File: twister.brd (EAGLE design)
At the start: 101.6 x 81.3 mm, 30 parts, among them IC1 A3967SLB, U2 ARDUINO_SHIELDNOHOLES

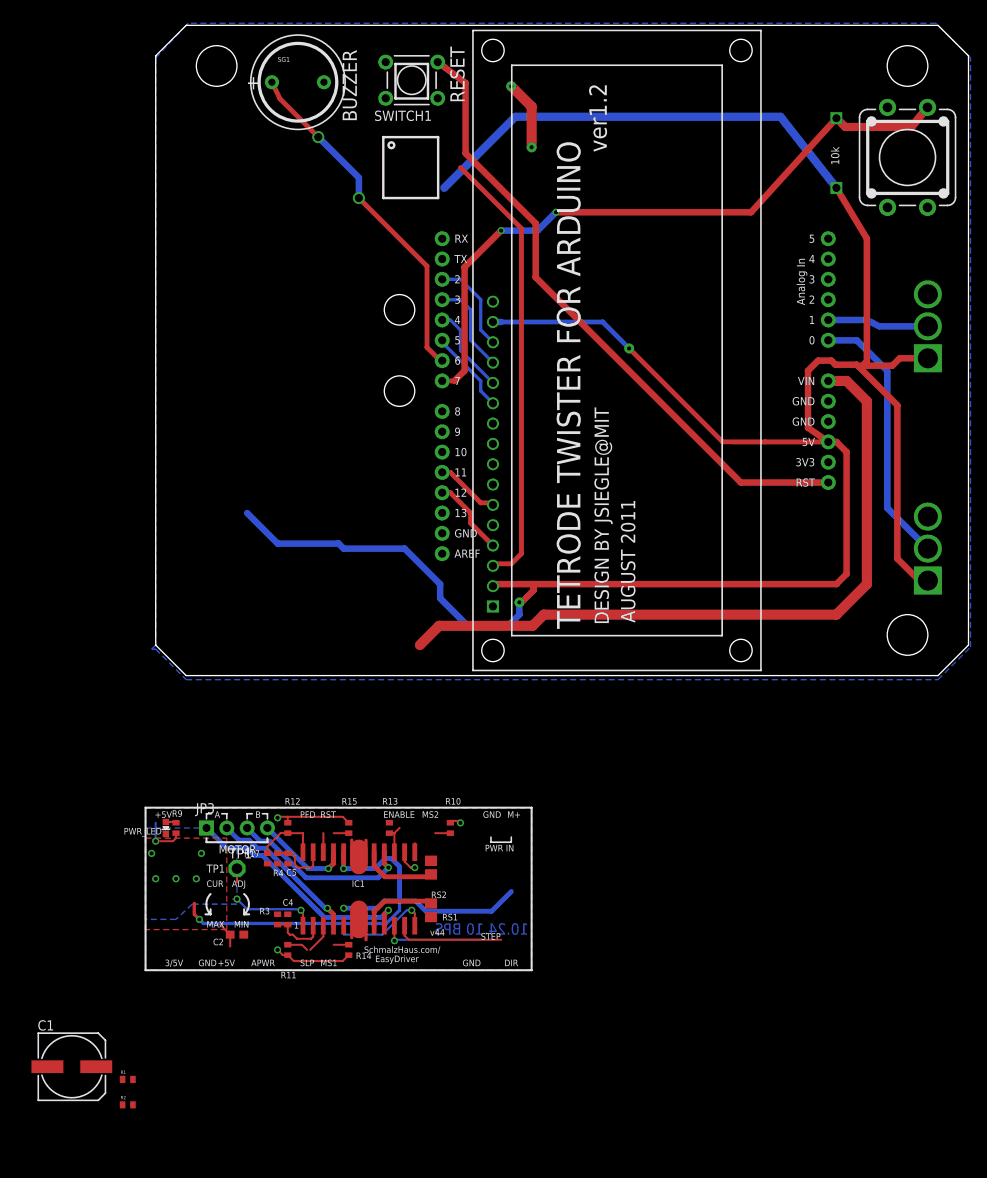
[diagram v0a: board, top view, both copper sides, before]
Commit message: Added stepper motor.
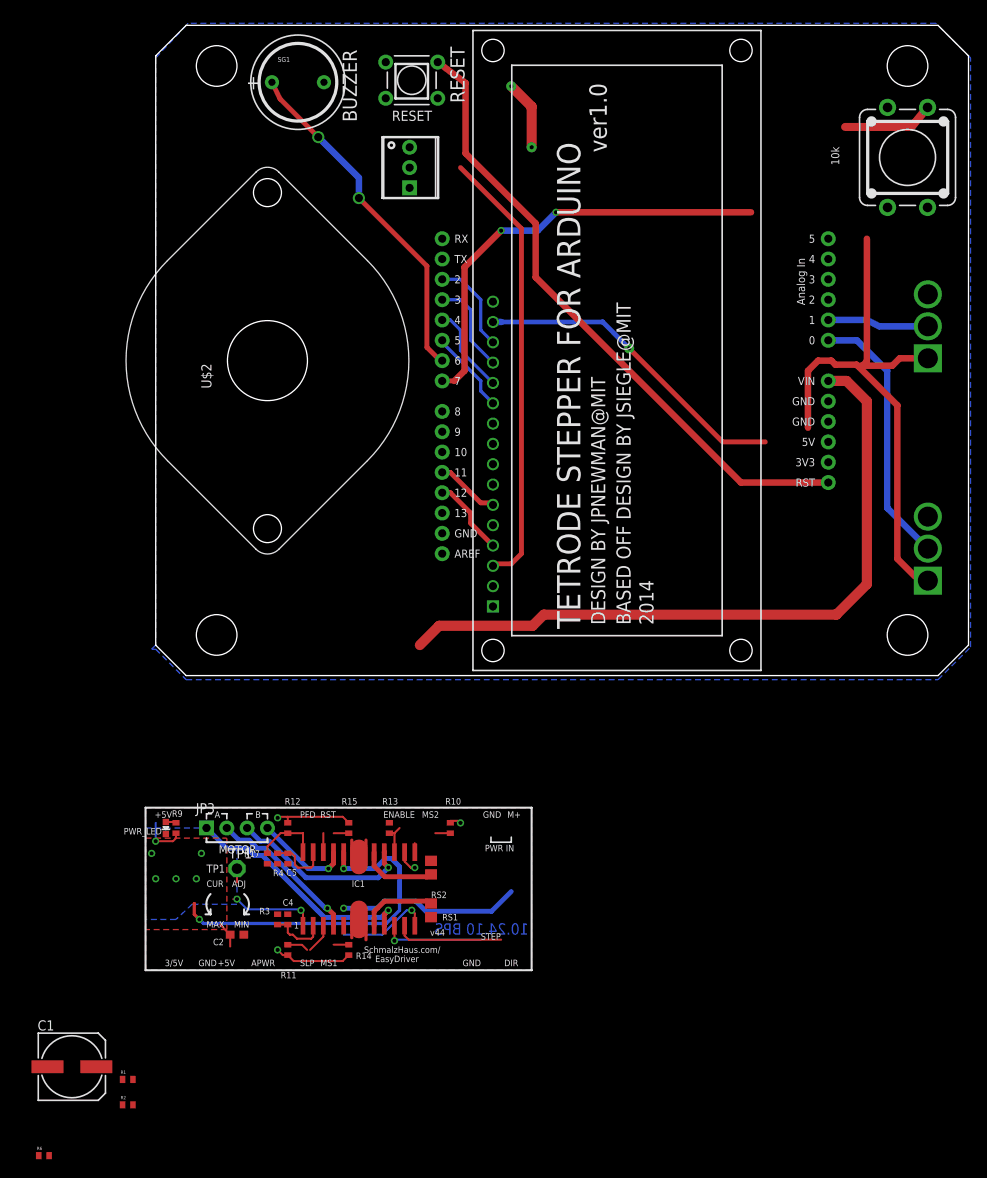
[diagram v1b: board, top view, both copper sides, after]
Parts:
- removed U$9: 10K, josh:RESISTOR
- added R56: CONTRAST, sparkfun:3362U-2
- added R6: 10K, SparkFun03_30_09:C0402
- added U$2: STEPPER_ST-PM35, twister:ST-PM35-15-11C
- RESET: value SWITCH-MOMENTARY-2PTH -> 2PTH
- S1: value SWITCH-MOMENTARY-212MM -> 212MM
- renumbered SWITCH1 to RESET
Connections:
- removed net VCC: C2.1, IC1.14, R10.2, R11.2, R12.2, R14.2, R15.2, R2.1, R9.2, U$1.15, U$10.LEFT, U$11.LEFT, U$9.P$1, U2.5V
- new net +5V: C2.1, IC1.14, R10.2, R11.2, R12.2, R14.2, R15.2, R2.1, R56.1, R6.1, R9.2, U$1.15, U$10.LEFT, U$11.LEFT
- net GND: now also R56.3
- net N$12: now also R6.2; no longer U$9.P$2
- net VO: now also R56.2
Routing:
- net VCC: track 328.3 -> 0.00 mm, vias 7 -> 0
- net +5V: track 0.00 -> 143.5 mm, vias 0 -> 6
- net N$12: track 83.8 -> 66.4 mm
- added copper zone on layer 16, net +5V
- removed copper zone on layer 16, net VCC
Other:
- board text added: "2014"
- board text added: "BASED OFF DESIGN BY JSIEGLE@MIT"
- board text added: "DESIGN BY JPNEWMAN@MIT"
- board text added: "TETRODE STEPPER FOR ARDUINO"
- board text added: "ver1.0"
- board text removed: "AUGUST 2011"
- board text removed: "DESIGN BY JSIEGLE@MIT"
- board text removed: "TETRODE TWISTER FOR ARDUINO"
- board text removed: "ver1.2"

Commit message: Everything should be set for final layout.
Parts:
- removed PWR_LED: YELLOW, SparkFun03_30_09:LED-0603
- removed R56: CONTRAST, sparkfun:3362U-2
- removed R9: 1K, SparkFun03_30_09:C0402
- removed S1: 212MM, sparkfun:TACTILE-PTH-12MM
- removed SG1: BUZZERPTH, sparkfun:BUZZER-12MM
- removed U$1: LCD-16X2, sparkfun:LCD-16X2
- removed U$2: STEPPER_ST-PM35, twister:ST-PM35-15-11C
- added BUZZER: SG1, twister_clean:BUZZER-12MM
- added CONTRAST: 10k, twister_clean:3362U-2
- added LCD_MODULE: LCD-16X2, twister_clean:LCD-16X2
- added START: 212MM, twister_clean:TACTILE-PTH-12MM
- added STEPPER: ST-PM35, twister:ST-PM35-15-11C
- C2: device rcl:C0603 -> twister_clean:0805
- C4, C5, R1, R10, R11, R12, R13, R14, R15, R17, R2, R3, R4, R6: device SparkFun03_30_09:C0402 -> twister_clean:0603
- RESET: device sparkfun:TACTILE-PTH -> twister_clean:TACTILE-PTH
- RS1, RS2: device rcl:R0805 -> twister_clean:1206
- U$10, U$11: device josh:LARGE_POT -> twister_clean:LARGE_POT
- U2: device sparkfun:DUEMILANOVE_SHIELD_NOHOLES -> twister_clean:DUEMILANOVE_SHIELD_NOHOLES
- moved C1 114.9 mm to (83.5, 17.1)
- moved RS1 51.3 mm to (29.3, 21.7), turned to 180 degrees
- moved RS2 46.9 mm to (24.0, 21.7), turned to 0 degrees
- moved R14 46.8 mm to (34.3, 11.4), turned to 0 degrees
- moved R10 46.7 mm to (19.1, 24.1), turned to 180 degrees
- moved R11 42.0 mm to (34.3, 3.81), turned to 0 degrees
- moved IC1 39.4 mm to (26.7, 12.7), turned to 90 degrees
- moved C2 37.2 mm to (32.4, -2.54), turned to 90 degrees
- moved C4 37.0 mm to (30.5, 3.81), turned to 180 degrees
- moved R13 37.0 mm to (19.1, 16.5), turned to 0 degrees
- moved R3 36.4 mm to (30.5, 2.54), turned to 0 degrees
- moved R15 30.9 mm to (19.1, 11.4), turned to 180 degrees
- moved C5 27.4 mm to (22.9, 3.81), turned to 0 degrees
- moved R4 26.5 mm to (22.9, 2.54), turned to 180 degrees
- moved R17 25.7 mm to (22.9, 1.27), turned to 180 degrees
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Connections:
- removed net N$17: PWR_LED.A, R9.1
- removed net N$24: U$1.1, U$1.5
- removed net V+: C1.+
- net +5V: now also CONTRAST.1, LCD_MODULE.15, U2.5V; no longer R56.1, R9.2, U$1.15
- net D6: now also BUZZER.-; no longer SG1.-
- net GND: now also BUZZER.+, CONTRAST.3, LCD_MODULE.1, LCD_MODULE.16, LCD_MODULE.5, START.3; no longer PWR_LED.C, R56.3, S1.3, SG1.+, U$1.16
- net N$12: now also START.1; no longer S1.1
- net N$4: now also LCD_MODULE.4; no longer U$1.4
- net N$5: now also LCD_MODULE.6; no longer U$1.6
- net N$6: now also LCD_MODULE.11; no longer U$1.11
- net N$7: now also LCD_MODULE.12; no longer U$1.12
- net N$8: now also LCD_MODULE.13; no longer U$1.13
- net N$9: now also LCD_MODULE.14; no longer U$1.14
- net VDD: now also LCD_MODULE.2; no longer U$1.2
- net VIN: now also C1.+
- net VO: now also CONTRAST.2, LCD_MODULE.3; no longer R56.2, U$1.3
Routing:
- net +5V: track 143.5 -> 72.7 mm, vias 6 -> 4
- net VIN: track 154.3 -> 93.0 mm
- net RESET: track 83.7 -> 79.5 mm
- net N$14: track 12.8 -> 10.6 mm
- net MS1: track 13.8 -> 11.9 mm
- net N$17: track 1.37 -> 0.00 mm
- net ENABLE: track 3.92 -> 3.06 mm
- net D6: track 43.3 -> 43.5 mm, vias 2 -> 0
- removed copper zone on layer 16, net +5V
- removed copper zone on layer 1, net 5V_ALT
- removed copper zone on layer 16, net 5V_ALT
- removed copper zone on layer 1, net GND
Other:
- board text added: "BASED ON DESIGN BY JSIEGLE@MIT"
- board text removed: "+"
- board text removed: "10.24.10 BPS"
- board text removed: "10k"
- board text removed: "3/5V"
- board text removed: "ADJ"
- board text removed: "APWR"
- board text removed: "BASED OFF DESIGN BY JSIEGLE@MIT"
- board text removed: "BUZZER"
- board text removed: "CUR"
- board text removed: "DIR"
- board text removed: "EasyDriver"
- board text removed: "GND"
- board text removed: "M+"
- board text removed: "MAX"
- board text removed: "MIN"
- board text removed: "MS1"
- board text removed: "PWR IN"
- board text removed: "RESET"
- board text removed: "SLP"
- board text removed: "SchmalzHaus.com/"
- board text removed: "TP1"

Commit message: Halfway through layout.
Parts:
- removed TP1: TPPAD1-13, testpad:P1-13
- moved R6 163.9 mm to (86.0, 69.8), turned to 270 degrees
- moved R2 66.0 mm to (31.1, 2.54)
- moved R1 65.1 mm to (34.3, 2.54)
- moved C2 50.2 mm to (80.6, 11.4), turned to 0 degrees
- moved JP3 22.6 mm to (5.08, 11.4)
- moved C4 4.58 mm to (34.3, 6.35), turned to 0 degrees
- moved C5 4.58 mm to (19.1, 6.35), turned to 180 degrees
- moved R10 4.45 mm to (19.1, 19.7)
- moved R11 4.45 mm to (34.3, 8.26)
- moved R3 4.26 mm to (34.3, 4.45), turned to 180 degrees
- moved R4 4.26 mm to (19.1, 4.45), turned to 0 degrees
- moved R15 3.17 mm to (19.1, 8.26)
- moved R17 1.42 mm to (22.2, 2.54)
- moved R12 1.27 mm to (19.1, 2.54)
- moved R14 1.27 mm to (34.3, 10.2)
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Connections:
- net DIR: now also U2.A1; no longer U2.A3
- net ENABLE: now also U2.D8; no longer U2.D10
- net MS1: now also U2.D10; no longer U2.D8
- net N$10: now also U2.A4; no longer U2.A0
- net N$11: now also U2.A5; no longer U2.A1
- net N$14: no longer TP1.1
- net PFD: now also U2.A3; no longer U2.A2
- net STEP: now also U2.A2; no longer U2.A4
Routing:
- net RESET: track 79.5 -> 199.1 mm, vias 0 -> 1
- net PFD: track 8.62 -> 115.3 mm
- net STEP: track 12.7 -> 112.4 mm, vias 1 -> 0
- net DIR: track 13.5 -> 106.8 mm
- net +5V: track 72.7 -> 8.03 mm, vias 4 -> 0
- net GND: track 25.8 -> 0.00 mm, vias 2 -> 0
- net OUT1A: track 23.1 -> 0.20 mm, vias 1 -> 0
- net VIN: track 93.0 -> 112.2 mm
- net OUT2A: track 30.1 -> 12.0 mm
- net N$10: track 33.3 -> 50.4 mm
- net N$12: track 66.4 -> 83.1 mm
- net OUT2B: track 19.2 -> 2.76 mm
- net N$11: track 12.6 -> 26.5 mm
- net MS1: track 11.9 -> 0.00 mm, vias 1 -> 0
- net OUT1B: track 12.0 -> 1.43 mm, vias 1 -> 0
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- added copper zone on layer 1, net +5V
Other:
- board text removed: "STEP"
- board text removed: "v44"

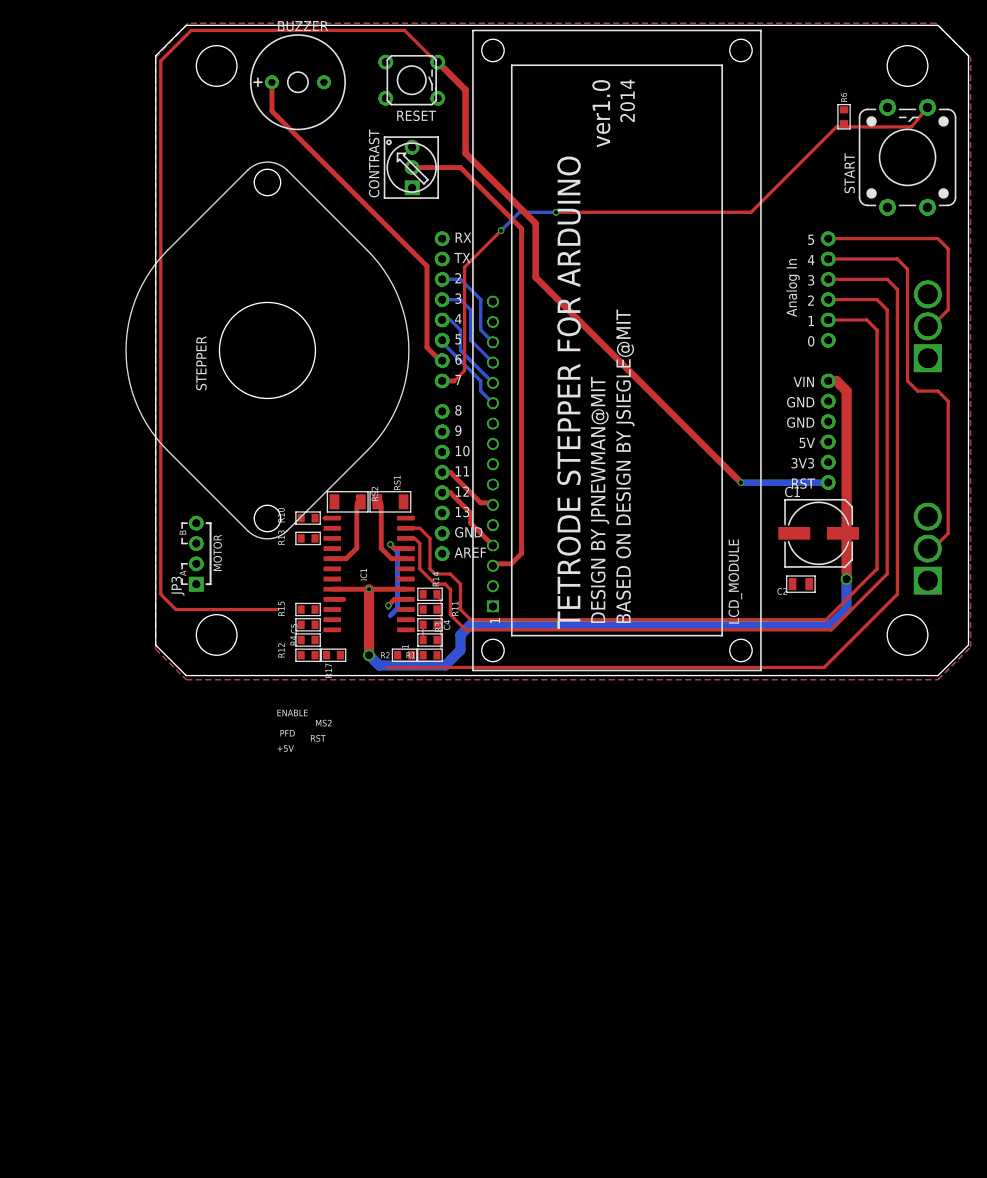
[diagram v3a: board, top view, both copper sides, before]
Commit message: Just about finished. Need to clean up aux materials so they actually match the pcb.
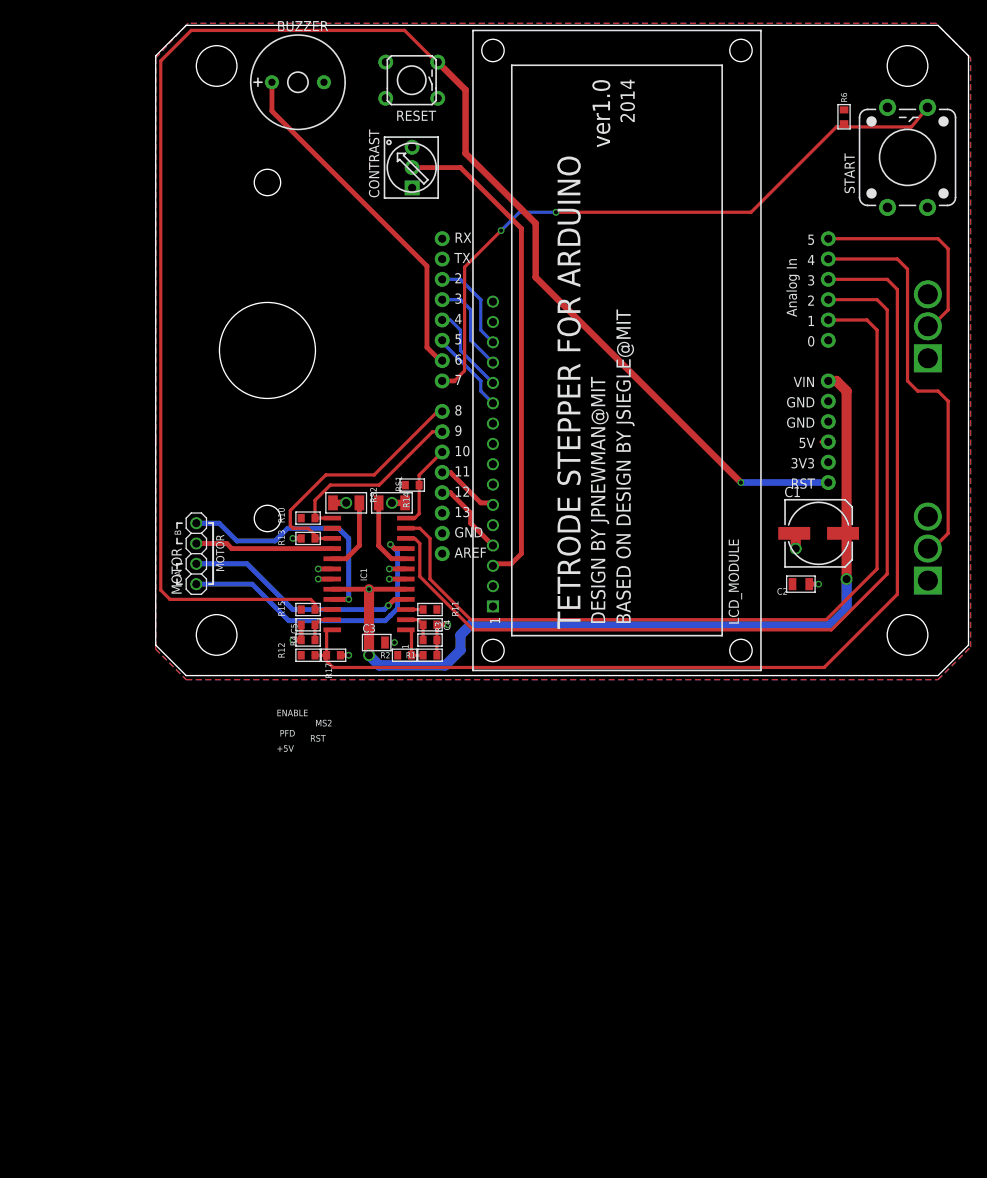
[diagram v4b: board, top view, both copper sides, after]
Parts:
- removed JP3: (no value), sparkfun:1X04_NO_SILK
- added C3: 1uf, twister_clean:0805
- added MOTOR: PINHD-1X4, twister_clean:1X04
- IC1: device Allegro:SO24W -> twister_clean:SO24W
- moved R14 13.8 mm to (32.1, 23.8), turned to 180 degrees
- moved RS1 0.23 mm to (29.5, 21.6)
- moved RS2 0.23 mm to (23.8, 21.6)
- flipped STEPPER to the bottom
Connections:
- removed net VDD: LCD_MODULE.2
- net +5V: now also LCD_MODULE.2
- net GND: now also C3.2
- net OUT1A: now also MOTOR.3; no longer JP3.3
- net OUT1B: now also MOTOR.4; no longer JP3.4
- net OUT2A: now also MOTOR.1; no longer JP3.1
- net OUT2B: now also MOTOR.2; no longer JP3.2
- net VIN: now also C3.1
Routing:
- net ENABLE: track 0.00 -> 32.2 mm
- net OUT1B: track 1.43 -> 32.3 mm, vias 0 -> 1
- net OUT2A: track 12.0 -> 38.4 mm
- net OUT2B: track 2.76 -> 29.1 mm
- net GND: track 0.00 -> 24.3 mm, vias 0 -> 13
- net MS2: track 1.12 -> 23.8 mm
- net OUT1A: track 0.20 -> 17.4 mm
- net PFD: track 115.3 -> 129.5 mm
- net MS1: track 0.00 -> 10.8 mm
- net +5V: track 8.03 -> 0.91 mm
- net RESET: track 199.1 -> 206.0 mm
- net N$14: track 0.00 -> 5.46 mm
- net N$13: track 0.00 -> 4.32 mm
- net N$2: track 1.90 -> 4.32 mm
- net SLEEP: track 0.03 -> 2.18 mm
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
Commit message: Finished rev 1.0 and sent to fab.
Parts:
- removed R15: 10K, twister_clean:0603
- removed R17: ???, twister_clean:0603
- removed U$10, U$11: LARGE_POT, twister_clean:LARGE_POT
- added R5, R7, R8, R9: 10K, twister_clean:0603
- C1: value 47uF -> 1uF; device cyclops:153CLV-0807 -> twister_clean:0805
- C2: value 1uf -> 47uF; device twister_clean:0805 -> cyclops:153CLV-0807
- C3: value 1uf -> 1uF
- R1: value 10K -> R12-0; device twister_clean:0603 -> twister_clean:LARGE_POT
- R13: value 10K -> ???
- R14, R6: value 10K -> 20K
- R2: value 11k -> R12-0; device twister_clean:0603 -> twister_clean:LARGE_POT
- R3: value 20K -> 10K
- R4: value 20K -> 11K
- moved R3 83.4 mm to (86.0, 69.8), turned to 270 degrees
- moved R6 83.4 mm to (34.3, 4.45), turned to 180 degrees
- moved R1 74.6 mm to (96.5, 43.7), turned to 90 degrees
- moved R2 66.8 mm to (96.5, 15.9), turned to 90 degrees
- moved C1 58.1 mm to (26.7, 2.86)
- moved C3 53.5 mm to (80.6, 11.4)
- moved R14 23.3 mm to (19.1, 4.45), turned to 0 degrees
- moved R11 17.6 mm to (19.1, 17.1)
- moved R12 17.1 mm to (19.1, 19.7)
- moved R4 15.4 mm to (34.3, 2.54), turned to 180 degrees
- moved R13 14.9 mm to (22.2, 2.54), turned to 180 degrees
- moved R10 11.4 mm to (19.1, 8.26)
- moved C2 6.73 mm to (82.9, 17.8)
- moved STEPPER 0.63 mm to (13.3, 40.6)
- moved RS1 0.32 mm to (29.5, 21.9)
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- renumbered U2 to U1
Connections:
- net +5V: now also C3.1, R1.LEFT, R2.LEFT, R3.1, R4.1, R7.2, R8.2, R9.2; no longer C2.1, R11.2, R14.2, R15.2, R2.1, R6.1, U$10.LEFT, U$11.LEFT
- net ENABLE: now also R11.2; no longer R13.2
- net GND: now also C1.2, C2.-, R1.RIGHT, R11.1, R14.1, R2.RIGHT, R5.2, R6.1; no longer C1.-, C2.2, R1.2, R17.1, R3.1, R4.1, U$10.RIGHT, U$11.RIGHT
- net MS1: now also R8.1; no longer R14.1
- net MS2: now also R12.1; no longer R10.1
- net N$10: now also R2.CENTER; no longer U$10.CENTER
- net N$11: now also R1.CENTER; no longer U$11.CENTER
- net N$12: now also R3.2; no longer R6.2
- net N$13: now also R14.2; no longer R4.2
- net N$14: now also R4.2, R5.1; no longer R1.1, R2.2
- net N$2: now also R6.2; no longer R3.2
- net PFD: now also R13.2, R9.1; no longer R12.1, R17.2
- net RESET: now also R10.1; no longer R15.1
- net SLEEP: now also R7.1; no longer R11.1
- net VIN: now also C1.1, C2.+; no longer C1.+, C3.1
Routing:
- net N$11: track 26.5 -> 22.0 mm
- net N$10: track 50.4 -> 46.4 mm
- net DIR: track 105.7 -> 102.6 mm, vias 0 -> 2
- net STEP: track 111.1 -> 108.6 mm, vias 0 -> 2
- net PFD: track 129.5 -> 127.0 mm, vias 0 -> 2
- net VIN: track 112.2 -> 114.5 mm
- net GND: track 24.3 -> 25.1 mm
- net N$9: track 11.8 -> 12.4 mm
- net D6: track 43.5 -> 43.8 mm, vias 0 -> 2
- net RESET: track 206.0 -> 206.3 mm, vias 1 -> 5
- net MS2: vias 0 -> 3
- net VO: vias 0 -> 1
- net OUT2B: vias 1 -> 2
- net ENABLE: vias 0 -> 3
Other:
- board text added: "BASED ON `TWISTER' BY JSIEGLE@MIT"
- board text added: "DESIGNED BY JPNEWMAN@MIT"
- board text removed: "+5V"
- board text removed: "1"
- board text removed: "BASED ON DESIGN BY JSIEGLE@MIT"
- board text removed: "DESIGN BY JPNEWMAN@MIT"
- board text removed: "ENABLE"
- board text removed: "MOTOR"
- board text removed: "MS2"
- board text removed: "PFD"
- board text removed: "RST"
